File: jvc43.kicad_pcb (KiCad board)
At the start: 6 copper layers, 101.6 x 50.8 mm, 143 parts, among them J201 8P8C_LED_Shielded, J301 8P8C_LED_Shielded, J401 USB_C_Receptacle_USB2.0, U201 LAN8810, U301 LAN8810, U401 LTC3622*DE, X101 25 MHz

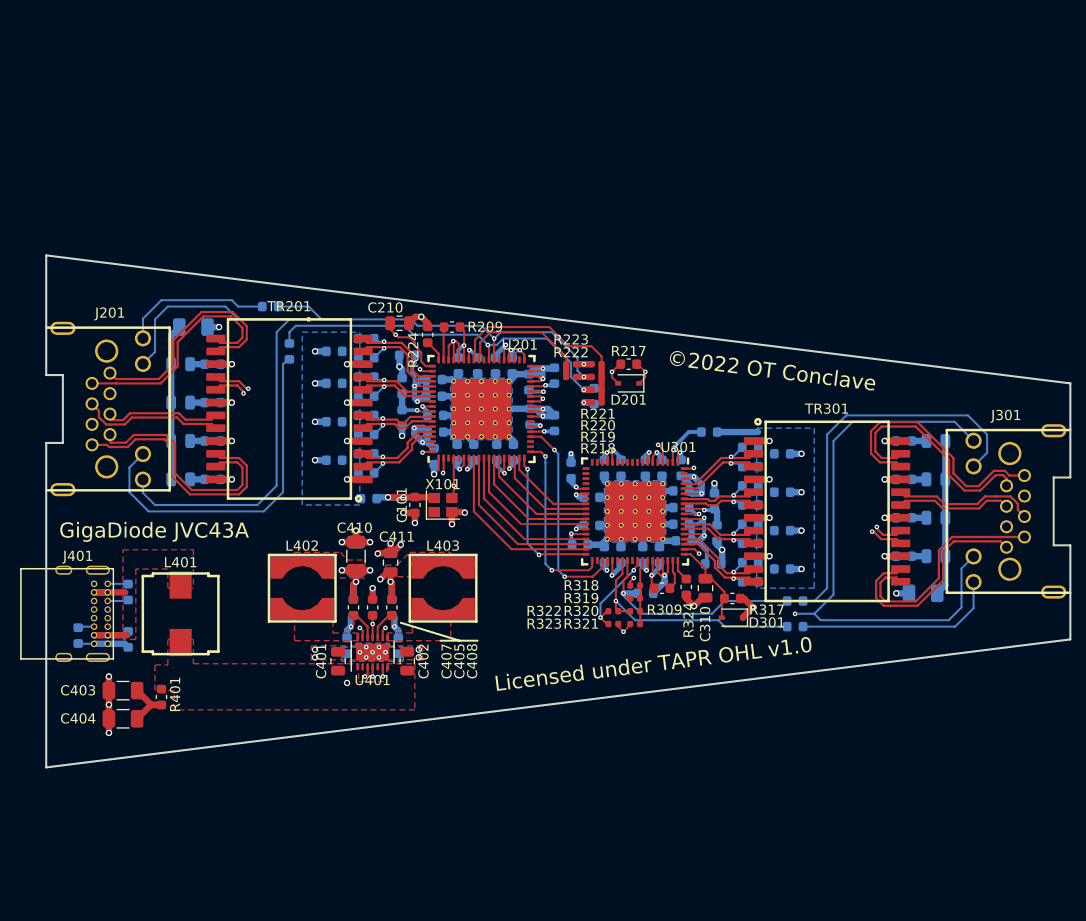
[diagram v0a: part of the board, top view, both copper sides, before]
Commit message: Forward progress: - Ripped up a good chunk of the old place&route around the PHYs - Swizzled graphical placement of LAN8831 diff pair pins, to make the trace   routing be straight-thru.  This also involved swapping the polarity I'm   feeding into the magnetics.  Bonus: the magnetics-to-RJ45 is now straight,   instead of having to go around the back sides! - Adjusted some default trace spacings because of the tiny 0.4mm QFN:   - Switched default traces from 8mil to 7.8mil   - Switched diff pairs from 8.8/8.1 to 7.4/7.8 - Whoops, not all the 0.1uF decoupling caps were 0402 sized yet - Filled in a lot of specific vendor P/Ns for resistors & capacitors, to make   dealing with assembly houses easier
PHY1 has all its close-in decoupling caps placed & routed, PHY2 does not yet.
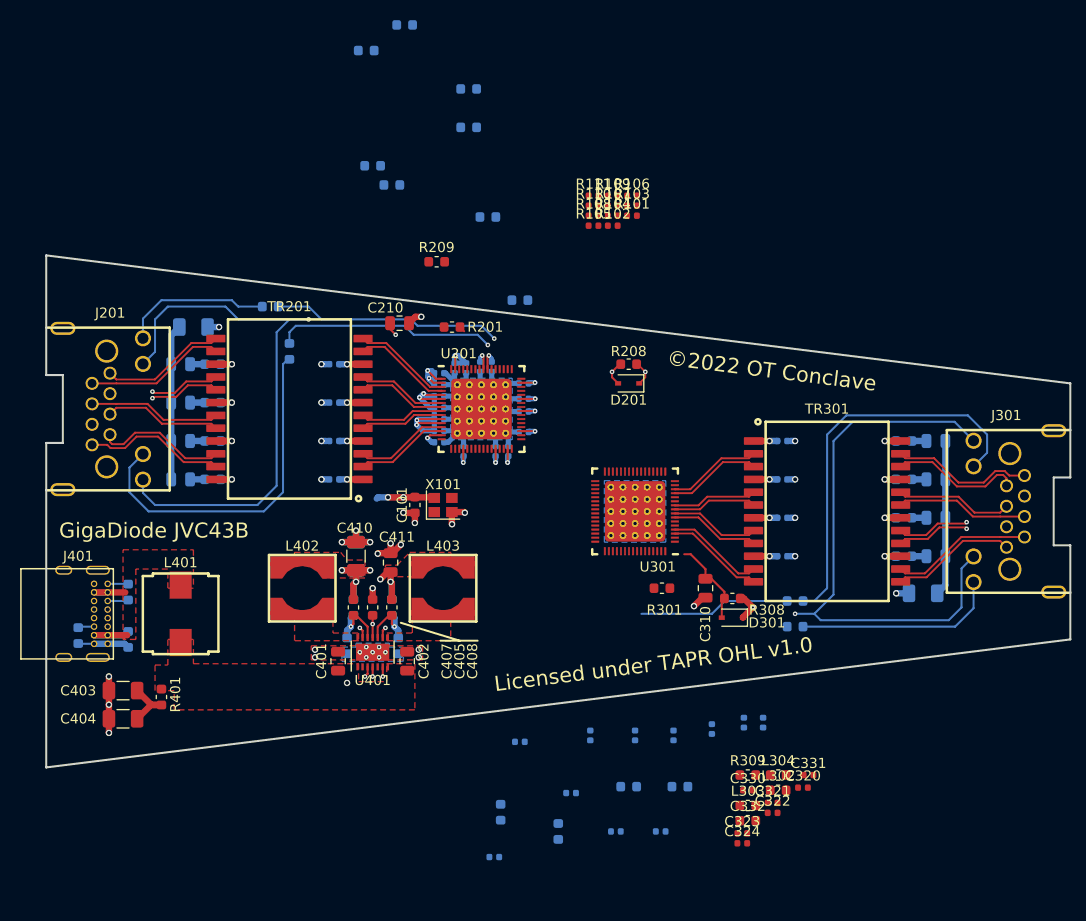
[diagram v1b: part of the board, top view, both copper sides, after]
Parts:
- removed the L201 at (57.4, 49.5)
- removed the L301 at (91.2, 42.9)
- removed the R201 at (57.1, 33.7)
- removed the R202 at (57.1, 35.6)
- removed the R203 at (57.1, 37.5)
- removed the R204 at (57.1, 39.4)
- removed the R205 at (57.1, 41.3)
- removed the R206 at (57.1, 43.2)
- removed the R207 at (57.1, 45.1)
- removed the R208 at (57.1, 47.0)
- removed R216, R316: 5k1, Resistor_SMD:R_0603_1608Metric
- removed R218, R223, R318, R323: 0, Resistor_SMD:R_0402_1005Metric
- removed R219, R220, R221, R222, R319, R320, R321, R322: dnp, Resistor_SMD:R_0402_1005Metric
- removed R224, R324: 8.06k, Resistor_SMD:R_0603_1608Metric
- removed the R301 at (95.2, 57.8)
- removed the R302 at (95.2, 55.9)
- removed the R303 at (95.2, 54.0)
- removed the R304 at (95.2, 52.1)
- removed the R305 at (95.2, 50.2)
- removed the R306 at (95.2, 48.3)
- removed the R307 at (95.2, 46.4)
- removed the R308 at (95.2, 44.5)
- added C225: 0.1u, Capacitor_SMD:C_0402_1005Metric, B.Cu at (64.4, 39.4)
- added C230: 10n, Capacitor_SMD:C_0402_1005Metric, B.Cu at (65.9, 36.6)
- added C231: 0.1u, Capacitor_SMD:C_0402_1005Metric, B.Cu at (67.1, 36.6)
- added C232: 4.7u, Capacitor_SMD:C_0603_1608Metric, B.Cu at (61.0, 2.54)
- added C325: 0.1u, Capacitor_SMD:C_0402_1005Metric, B.Cu at (91.4, 72.4)
- added C330: 10n, Capacitor_SMD:C_0402_1005Metric, F.Cu at (95.0, 78.5)
- added C331: 0.1u, Capacitor_SMD:C_0402_1005Metric, F.Cu at (101.0, 77.0)
- added C332: 4.7u, Capacitor_SMD:C_0603_1608Metric, F.Cu at (95.0, 81.5)
- added L202: 470 ohm, Inductor_SMD:L_0603_1608Metric, B.Cu at (67.3, 12.7)
- added L204: 470 ohm, Inductor_SMD:L_0603_1608Metric, B.Cu at (57.1, 5.08)
- added L302: 470 ohm, Inductor_SMD:L_0603_1608Metric, F.Cu at (98.0, 78.5)
- added L304: 470 ohm, Inductor_SMD:L_0603_1608Metric, F.Cu at (98.0, 77.0)
- added R101: 22, Resistor_SMD:R_0402_1005Metric, F.Cu at (83.5, 21.5)
- added R102: 22, Resistor_SMD:R_0402_1005Metric, F.Cu at (81.6, 22.5)
- added R103: 22, Resistor_SMD:R_0402_1005Metric, F.Cu at (83.5, 20.5)
- added R104: 22, Resistor_SMD:R_0402_1005Metric, F.Cu at (81.6, 21.5)
- added R105: 22, Resistor_SMD:R_0402_1005Metric, F.Cu at (79.7, 22.5)
- added R106: 22, Resistor_SMD:R_0402_1005Metric, F.Cu at (83.5, 19.5)
- added R107: 22, Resistor_SMD:R_0402_1005Metric, F.Cu at (81.6, 20.5)
- added R108: 22, Resistor_SMD:R_0402_1005Metric, F.Cu at (79.7, 21.5)
- added R109: 22, Resistor_SMD:R_0402_1005Metric, F.Cu at (81.6, 19.5)
- added R110: 22, Resistor_SMD:R_0402_1005Metric, F.Cu at (79.7, 20.5)
- added R111: 22, Resistor_SMD:R_0402_1005Metric, F.Cu at (79.7, 19.5)
- added R209: 6.04k, Resistor_SMD:R_0603_1608Metric, F.Cu at (64.1, 26.0)
- added R309: 6.04k, Resistor_SMD:R_0603_1608Metric, F.Cu at (95.0, 77.0)
- C201, C202, C203, C204, C301, C302, C303, C304: value 22n -> 0.1u; footprint Capacitor_SMD:C_0603_1608Metric -> Capacitor_SMD:C_0402_1005Metric
- C211, C219, C311, C319: value 10n -> 10u
- C212, C213, C214, C215, C216, C217, C218, C220, C221, C222, C223, C224, C226, C227, C228, C312, C313, C314, C315, C316, C317, C318, C326, C327, C328: value 10n -> 0.1u; footprint Capacitor_SMD:C_0603_1608Metric -> Capacitor_SMD:C_0402_1005Metric
- C229: renamed from C225; value 10n -> 10u
- C320, C321, C322, C323, C324: value 10n -> 0.1u; footprint Capacitor_SMD:C_0603_1608Metric -> Capacitor_SMD:C_0402_1005Metric; moved to F.Cu
- C329: renamed from C325; value 10n -> 10u
- L303: moved to F.Cu
- R208: renamed from R217; value 5k1 -> 10k
- R308: renamed from R317; value 5k1 -> 10k
- R404: value 100k -> 84.5k
- U201, U301: value LAN8810 -> LAN8831; footprint myfp:QFN-72-1EP_10x10mm_P0.5mm_EP6x6mm_ThermalVias -> myfp:QFN-64-1EP_8x8mm_P0.4mm_EP6x6mm_ThermalVias
- moved C313 40.8 mm to (69.8, 85.1)
- moved C322 38.1 mm to (97.5, 80.7), turned to 0 degrees
- moved C323 36.5 mm to (94.5, 82.7)
- moved C321 35.6 mm to (97.5, 79.7), turned to 0 degrees
- moved C324 34.9 mm to (94.5, 83.7)
- moved C328 33.2 mm to (86.4, 82.5), turned to 0 degrees
- moved L203 30.2 mm to (67.3, 8.89), turned to 0 degrees
- moved C312 28.8 mm to (77.5, 78.7)
- moved C318 28.7 mm to (81.9, 82.5)
- moved C327 28.2 mm to (72.4, 73.7), turned to 0 degrees
- moved C319 28.2 mm to (70.5, 80.6)
- moved C329 27.8 mm to (76.2, 82.5)
- moved L303 27.2 mm to (95.0, 80.0), turned to 0 degrees
- moved C320 27.1 mm to (100.5, 78.2), turned to 0 degrees
- moved C316 27.0 mm to (87.6, 73.0)
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- renumbered L202 to L201, L302 to L301, R209 to R201, R210 to R202, R211 to R203, R212 to R204, R213 to R205, R214 to R206, R215 to R207, R309 to R301, R310 to R302, R311 to R303, R312 to R304, R313 to R305, R314 to R306, R315 to R307
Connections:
- C201 pad 1: /Ethernet1/VDD_ETH -> /Ethernet1/ETH_CR3
- C202 pad 1: /Ethernet1/VDD_ETH -> /Ethernet1/ETH_CR2
- C203 pad 1: /Ethernet1/VDD_ETH -> /Ethernet1/ETH_CR1
- C204 pad 1: /Ethernet1/VDD_ETH -> /Ethernet1/ETH_CR0
- C211 pad 1: /Ethernet1/VDD12A -> /Ethernet1/VDDAH
- C212 pad 1: /Ethernet1/VDD12A -> /Ethernet1/VDDAH
- C213 pad 1: /Ethernet1/VDD12A -> /Ethernet1/VDDAH
- C214 pad 1: /Ethernet1/VDD12A -> /Ethernet1/VDDAH
- C215 pad 1: +2V5 -> /Ethernet1/VDD
- C216 pad 1: +2V5 -> /Ethernet1/VDD
- C217 pad 1: +2V5 -> /Ethernet1/VDD
- C218 pad 1: +2V5 -> /Ethernet1/VDD
- C219 pad 1: +2V5 -> /Ethernet1/VDD
- C221 pad 1: +1V2 -> +2V5
- C222 pad 1: +1V2 -> +2V5
- C223 pad 1: +1V2 -> +2V5
- C224 pad 1: +1V2 -> +2V5
- C226 pad 1: +1V2 -> /Ethernet1/VDDAL
- C227 pad 1: +1V2 -> /Ethernet1/VDDAL
- C228 pad 1: /Ethernet1/VDD12PLL -> /Ethernet1/VDDAL
- C229 pad 1: +1V2 -> /Ethernet1/VDDAL
- C301 pad 1: /Ethernet2/VDD_ETH -> /Ethernet2/ETH_CR3
- C302 pad 1: /Ethernet2/VDD_ETH -> /Ethernet2/ETH_CR2
- C303 pad 1: /Ethernet2/VDD_ETH -> /Ethernet2/ETH_CR1
- C304 pad 1: /Ethernet2/VDD_ETH -> /Ethernet2/ETH_CR0
- C311 pad 1: /Ethernet2/VDD12A -> /Ethernet2/VDDAH
- C312 pad 1: /Ethernet2/VDD12A -> /Ethernet2/VDDAH
- C313 pad 1: /Ethernet2/VDD12A -> /Ethernet2/VDDAH
- C314 pad 1: /Ethernet2/VDD12A -> /Ethernet2/VDDAH
- C315 pad 1: +2V5 -> /Ethernet2/VDD
- C316 pad 1: +2V5 -> /Ethernet2/VDD
- C317 pad 1: +2V5 -> /Ethernet2/VDD
- C318 pad 1: +2V5 -> /Ethernet2/VDD
- C319 pad 1: +2V5 -> /Ethernet2/VDD
- C321 pad 1: +1V2 -> +2V5
- C322 pad 1: +1V2 -> +2V5
- C323 pad 1: +1V2 -> +2V5
- C324 pad 1: +1V2 -> +2V5
- C326 pad 1: +1V2 -> /Ethernet2/VDDAL
- C327 pad 1: +1V2 -> /Ethernet2/VDDAL
- C328 pad 1: /Ethernet2/VDD12PLL -> /Ethernet2/VDDAL
- C329 pad 1: +1V2 -> /Ethernet2/VDDAL
- C407 pad 1: +1V2 -> +1V1
- C409 pad 1: +1V2 -> +1V1
- C410 pad 1: +1V2 -> +1V1
- L201 pad 1: +1V2 -> +2V5
- L201 pad 2: /Ethernet1/VDD12A -> /Ethernet1/VDDAH
- L203 pad 1: +1V2 -> /Ethernet1/VDDAL
- L203 pad 2: /Ethernet1/VDD12PLL -> +1V1
- L301 pad 1: +1V2 -> +2V5
- L301 pad 2: /Ethernet2/VDD12A -> /Ethernet2/VDDAH
- L303 pad 1: +1V2 -> /Ethernet2/VDDAL
- L303 pad 2: /Ethernet2/VDD12PLL -> +1V1
- L402 pad 1: +1V2 -> +1V1
- R201 pad 2: +2V5 -> /Ethernet1/VDDVARIO
- R301 pad 2: +2V5 -> /Ethernet2/VDDVARIO
- R404 pad 1: +1V2 -> +1V1
- TR201 pad 1: /Ethernet1/VDD_ETH -> /Ethernet1/ETH_CR3
- TR201 pad 10: /Ethernet1/VDD_ETH -> /Ethernet1/ETH_CR0
- TR201 pad 11: /Ethernet1/ETH_TR0+ -> /Ethernet1/ETH_TR0-
- TR201 pad 12: /Ethernet1/ETH_TR0- -> /Ethernet1/ETH_TR0+
- TR201 pad 13: /Ethernet1/ETH_TX0- -> /Ethernet1/ETH_TX0+
- TR201 pad 14: /Ethernet1/ETH_TX0+ -> /Ethernet1/ETH_TX0-
- TR201 pad 16: /Ethernet1/ETH_TX1- -> /Ethernet1/ETH_TX1+
- TR201 pad 17: /Ethernet1/ETH_TX1+ -> /Ethernet1/ETH_TX1-
- TR201 pad 19: /Ethernet1/ETH_TX2- -> /Ethernet1/ETH_TX2+
- TR201 pad 2: /Ethernet1/ETH_TR3+ -> /Ethernet1/ETH_TR3-
- TR201 pad 20: /Ethernet1/ETH_TX2+ -> /Ethernet1/ETH_TX2-
- TR201 pad 22: /Ethernet1/ETH_TX3- -> /Ethernet1/ETH_TX3+
- TR201 pad 23: /Ethernet1/ETH_TX3+ -> /Ethernet1/ETH_TX3-
- TR201 pad 3: /Ethernet1/ETH_TR3- -> /Ethernet1/ETH_TR3+
- TR201 pad 4: /Ethernet1/VDD_ETH -> /Ethernet1/ETH_CR2
- TR201 pad 5: /Ethernet1/ETH_TR2+ -> /Ethernet1/ETH_TR2-
- TR201 pad 6: /Ethernet1/ETH_TR2- -> /Ethernet1/ETH_TR2+
- TR201 pad 7: /Ethernet1/VDD_ETH -> /Ethernet1/ETH_CR1
- TR201 pad 8: /Ethernet1/ETH_TR1+ -> /Ethernet1/ETH_TR1-
- TR201 pad 9: /Ethernet1/ETH_TR1- -> /Ethernet1/ETH_TR1+
- TR301 pad 1: /Ethernet2/VDD_ETH -> /Ethernet2/ETH_CR3
- TR301 pad 10: /Ethernet2/VDD_ETH -> /Ethernet2/ETH_CR0
- TR301 pad 11: /Ethernet2/ETH_TR0+ -> /Ethernet2/ETH_TR0-
- TR301 pad 12: /Ethernet2/ETH_TR0- -> /Ethernet2/ETH_TR0+
- TR301 pad 13: /Ethernet2/ETH_TX0- -> /Ethernet2/ETH_TX0+
- TR301 pad 14: /Ethernet2/ETH_TX0+ -> /Ethernet2/ETH_TX0-
- TR301 pad 16: /Ethernet2/ETH_TX1- -> /Ethernet2/ETH_TX1+
- TR301 pad 17: /Ethernet2/ETH_TX1+ -> /Ethernet2/ETH_TX1-
- TR301 pad 19: /Ethernet2/ETH_TX2- -> /Ethernet2/ETH_TX2+
- TR301 pad 2: /Ethernet2/ETH_TR3+ -> /Ethernet2/ETH_TR3-
- TR301 pad 20: /Ethernet2/ETH_TX2+ -> /Ethernet2/ETH_TX2-
- TR301 pad 22: /Ethernet2/ETH_TX3- -> /Ethernet2/ETH_TX3+
- TR301 pad 23: /Ethernet2/ETH_TX3+ -> /Ethernet2/ETH_TX3-
- TR301 pad 3: /Ethernet2/ETH_TR3- -> /Ethernet2/ETH_TR3+
- TR301 pad 4: /Ethernet2/VDD_ETH -> /Ethernet2/ETH_CR2
- TR301 pad 5: /Ethernet2/ETH_TR2+ -> /Ethernet2/ETH_TR2-
- TR301 pad 6: /Ethernet2/ETH_TR2- -> /Ethernet2/ETH_TR2+
- TR301 pad 7: /Ethernet2/VDD_ETH -> /Ethernet2/ETH_CR1
- TR301 pad 8: /Ethernet2/ETH_TR1+ -> /Ethernet2/ETH_TR1-
- TR301 pad 9: /Ethernet2/ETH_TR1- -> /Ethernet2/ETH_TR1+
- U201 pad 1: GND -> /Ethernet1/VDDAH
- U201 pad 10: /Ethernet1/RXD2 -> /Ethernet1/ETH_TR2-
- U201 pad 11: /Ethernet1/RXD3 -> /Ethernet1/VDDAL
- U201 pad 12: /Ethernet1/RXD4 -> /Ethernet1/VDDAL
- U201 pad 13: /Ethernet1/RXD5 -> /Ethernet1/ETH_TR3+
- U201 pad 14: +2V5 -> /Ethernet1/ETH_TR3-
- U201 pad 15: +1V2 -> /Ethernet1/VDDAH
- U201 pad 16: /Ethernet1/RXD6 -> /Ethernet1/LED5
- U201 pad 17: /Ethernet1/RXD7 -> /Ethernet1/LED4
- U201 pad 18: /EN_W2B -> /Ethernet1/LED3
- U201 pad 19: /ER_W2B -> /Ethernet1/LED2
- U201 pad 2: +2V5 -> /Ethernet1/VDDAH
- U201 pad 20: /Ethernet1/CRS -> +2V5
- U201 pad 21: /Ethernet1/COL -> /Ethernet1/LED1
- U201 pad 22: /CLK_W2B -> GND
- U201 pad 23: +2V5 -> GND
- U201 pad 24: +1V2 -> GND
- U201 pad 25: Net-(U201-Pad25) -> GND
- U201 pad 28: GND -> /Ethernet1/VDD
- U201 pad 3: /Ethernet1/TDO -> /Ethernet1/ETH_TR0+
- U201 pad 31: +1V2 -> +2V5
- U201 pad 32: +2V5 -> GND
- U201 pad 35: GND -> /Ethernet1/VDD
- U201 pad 36: GND -> /RXD7
- U201 pad 37: GND -> /RXD6
- U201 pad 38: /Ethernet1/TXCLK -> /RXD5
- U201 pad 39: GND -> /RXD4
- U201 pad 4: /Ethernet1/XI -> /Ethernet1/ETH_TR0-
- U201 pad 40: +1V2 -> +2V5
- U201 pad 41: +2V5 -> /RXD3
- U201 pad 42: /Ethernet1/ACT_LED -> /RXD2
- U201 pad 43: /Ethernet1/1000_LED -> /Ethernet1/VDD
- U201 pad 44: /Ethernet1/100_LED -> /RXD1
- U201 pad 45: /Ethernet1/10_LED -> /RXD0
- U201 pad 46: /Ethernet1/CONFIG3 -> /Ethernet1/RXDV
- U201 pad 47: /Ethernet1/CONFIG2 -> +2V5
- U201 pad 48: +1V2 -> /Ethernet1/RXER
- U201 pad 49: +2V5 -> /Ethernet1/RXCLK
- U201 pad 5: /Ethernet1/XO -> /Ethernet1/VDDAL
- U201 pad 50: GND -> /Ethernet1/CRS
- U201 pad 52: GND -> /Ethernet1/MDIO
- U201 pad 53: /Ethernet1/MDIO -> /Ethernet1/COL
- U201 pad 54: /Ethernet1/ETHRBIAS -> /Ethernet1/INT
- U201 pad 55: /Ethernet1/nRST -> /Ethernet1/VDD
- U201 pad 56: GND -> +2V5
- U201 pad 57: /Ethernet1/ETH_TR0- -> /Ethernet1/CLK125
- U201 pad 58: /Ethernet1/ETH_TR0+ -> /Ethernet1/nRST
- U201 pad 59: /Ethernet1/VDD12A -> /Ethernet1/TXCLK
- U201 pad 6: +2V5 -> /Ethernet1/VDDAL
- U201 pad 60: /Ethernet1/ETH_TR1- -> Net-(U201-Pad60)
- U201 pad 61: /Ethernet1/ETH_TR1+ -> /Ethernet1/XO
- U201 pad 62: /Ethernet1/VDD12A -> /Ethernet1/XI
- U201 pad 63: +1V2 -> /Ethernet1/VDDAL_PLL
- U201 pad 64: /Ethernet1/VDD12PLL -> /Ethernet1/ISET
- U201 pad 7: +1V2 -> /Ethernet1/ETH_TR1+
- U201 pad 8: /Ethernet1/RXD0 -> /Ethernet1/ETH_TR1-
- U201 pad 9: /Ethernet1/RXD1 -> /Ethernet1/ETH_TR2+
- U301 pad 1: GND -> /Ethernet2/VDDAH
- U301 pad 10: /Ethernet2/RXD2 -> /Ethernet2/ETH_TR2-
- U301 pad 11: /Ethernet2/RXD3 -> /Ethernet2/VDDAL
- U301 pad 12: /Ethernet2/RXD4 -> /Ethernet2/VDDAL
- U301 pad 13: /Ethernet2/RXD5 -> /Ethernet2/ETH_TR3+
- U301 pad 14: +2V5 -> /Ethernet2/ETH_TR3-
- U301 pad 15: +1V2 -> /Ethernet2/VDDAH
- U301 pad 16: /Ethernet2/RXD6 -> /Ethernet2/LED5
- U301 pad 17: /Ethernet2/RXD7 -> /Ethernet2/LED4
- U301 pad 18: /Ethernet2/RXDV -> /Ethernet2/LED3
- U301 pad 19: /Ethernet2/RXER -> /Ethernet2/LED2
- U301 pad 2: +2V5 -> /Ethernet2/VDDAH
- U301 pad 20: /Ethernet2/CRS -> +2V5
- U301 pad 21: /Ethernet2/COL -> /Ethernet2/LED1
- U301 pad 22: /Ethernet2/RXCLK -> /TXD0
- U301 pad 23: +2V5 -> /TXD1
- U301 pad 24: +1V2 -> /TXD2
- U301 pad 25: Net-(U301-Pad25) -> /TXD3
- U301 pad 26: /Ethernet1/RXD7 -> /TXD4
- U301 pad 27: /Ethernet1/RXD6 -> /TXD5
- U301 pad 28: /Ethernet1/RXD5 -> /Ethernet2/VDD
- U301 pad 29: /Ethernet1/RXD4 -> /TXD6
- U301 pad 3: /Ethernet2/TDO -> /Ethernet2/ETH_TR0+
- U301 pad 30: /Ethernet1/RXD3 -> /TXD7
- U301 pad 31: +1V2 -> +2V5
- U301 pad 32: +2V5 -> /ER_W2B
- U301 pad 33: /Ethernet1/RXD2 -> /CLK_W2B
- U301 pad 34: /Ethernet1/RXD1 -> /EN_W2B
- U301 pad 35: /Ethernet1/RXD0 -> /Ethernet2/VDD
- U301 pad 36: /EN_W2B -> /Ethernet2/RXD7
- U301 pad 37: /ER_W2B -> /Ethernet2/RXD6
- U301 pad 38: /Ethernet2/TXCLK -> /Ethernet2/RXD5
- U301 pad 39: /CLK_W2B -> /Ethernet2/RXD4
- U301 pad 4: /Ethernet1/XI -> /Ethernet2/ETH_TR0-
- U301 pad 40: +1V2 -> +2V5
- U301 pad 41: +2V5 -> /Ethernet2/RXD3
- U301 pad 42: /Ethernet2/ACT_LED -> /Ethernet2/RXD2
- U301 pad 43: /Ethernet2/1000_LED -> /Ethernet2/VDD
- U301 pad 44: /Ethernet2/100_LED -> /Ethernet2/RXD1
- U301 pad 45: /Ethernet2/10_LED -> /Ethernet2/RXD0
- U301 pad 46: /Ethernet2/CONFIG3 -> /Ethernet2/RXDV
- U301 pad 47: /Ethernet2/CONFIG2 -> +2V5
- U301 pad 48: +1V2 -> /Ethernet2/RXER
- U301 pad 49: +2V5 -> /Ethernet2/RXCLK
- U301 pad 5: /Ethernet2/XO -> /Ethernet2/VDDAL
- U301 pad 50: GND -> /Ethernet2/CRS
- U301 pad 52: GND -> /Ethernet2/MDIO
- U301 pad 53: /Ethernet2/MDIO -> /Ethernet2/COL
- U301 pad 54: /Ethernet2/ETHRBIAS -> /Ethernet2/INT
- U301 pad 55: /Ethernet2/nRST -> /Ethernet2/VDD
- U301 pad 56: GND -> +2V5
- U301 pad 57: /Ethernet2/ETH_TR0- -> /Ethernet2/CLK125
- U301 pad 58: /Ethernet2/ETH_TR0+ -> /Ethernet2/nRST
- U301 pad 59: /Ethernet2/VDD12A -> /Ethernet2/TXCLK
- U301 pad 6: +2V5 -> /Ethernet2/VDDAL
- U301 pad 60: /Ethernet2/ETH_TR1- -> Net-(U301-Pad60)
- U301 pad 61: /Ethernet2/ETH_TR1+ -> /Ethernet2/XO
- U301 pad 62: /Ethernet2/VDD12A -> /Ethernet1/XI
- U301 pad 63: +1V2 -> /Ethernet2/VDDAL_PLL
- U301 pad 64: /Ethernet2/VDD12PLL -> /Ethernet2/ISET
- U301 pad 7: +1V2 -> /Ethernet2/ETH_TR1+
- U301 pad 8: /Ethernet2/RXD0 -> /Ethernet2/ETH_TR1-
- U301 pad 9: /Ethernet2/RXD1 -> /Ethernet2/ETH_TR2+
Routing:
- net GND: track 239.9 -> 165.0 mm, vias 56 -> 39
- net +1V2: track 45.7 -> 0.00 mm, vias 19 -> 0
- net +2V5: track 66.1 -> 29.0 mm, vias 24 -> 11
- net /Ethernet1/XI: track 28.1 -> 0.00 mm, vias 2 -> 0
- net /Ethernet2/1000_LED: track 24.6 -> 0.00 mm, vias 1 -> 0
- net /Ethernet2/VDD12A: track 22.8 -> 0.00 mm, vias 4 -> 0
- net /Ethernet1/VDD12A: track 21.7 -> 0.00 mm, vias 4 -> 0
- net /Ethernet1/CONFIG2: track 20.9 -> 0.00 mm
- net /CLK_W2B: track 20.7 -> 0.00 mm, vias 2 -> 0
- net /Ethernet1/VDDAL: track 0.00 -> 20.4 mm, vias 0 -> 4
- net /ER_W2B: track 18.0 -> 0.00 mm, vias 2 -> 0
- net /Ethernet1/RXD0: track 18.0 -> 0.00 mm
- net /Ethernet1/RXD1: track 16.9 -> 0.00 mm
- net /Ethernet1/100_LED: track 38.0 -> 21.9 mm, vias 2 -> 1
- net /Ethernet1/RXD2: track 15.8 -> 0.00 mm
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- added copper zone on F.Cu, net +1V1
- added copper zone on L3.Cu, net +1V1
- removed copper zone on F.Cu, net +1V2
- removed copper zone on L3.Cu, net +1V2
- removed copper zone on L4.Cu, net /Ethernet1/VDD12A
- removed copper zone on B.Cu, net /Ethernet1/VDD_ETH
- removed copper zone on L4.Cu, net /Ethernet2/VDD12A
- removed copper zone on B.Cu, net /Ethernet2/VDD_ETH
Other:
- net class Default: clearance 0.2032 -> 0.19812; trace_width 0.2032 -> 0.19812
- net class Diff100: clearance 0.20574 -> 0.19812; trace_width 0.22352 -> 0.18796
- net class Phat25: clearance 0.2032 -> 0.19812
- net class UghClear removed
- rule trace_clearance: 0.2032 -> 0.19812
- board text added: "(11) IMPEDANCE: ALL 7.4 MIL WIDE / 7.8 MIL SPACE PAIRS ON LAYERS F/3 SHALL BE 100 OHMS +/- 10%. REFERENCE LAYER 2."
- board text added: "GigaDiode JVC43B"
- board text removed: "(11) IMPEDANCE: ALL 8.8 MIL WIDE / 8.1 MIL SPACE PAIRS ON LAYERS F/3 SHALL BE 100 OHMS +/- 10%. REFERENCE LAYER 2."
- board text removed: "GigaDiode JVC43A"

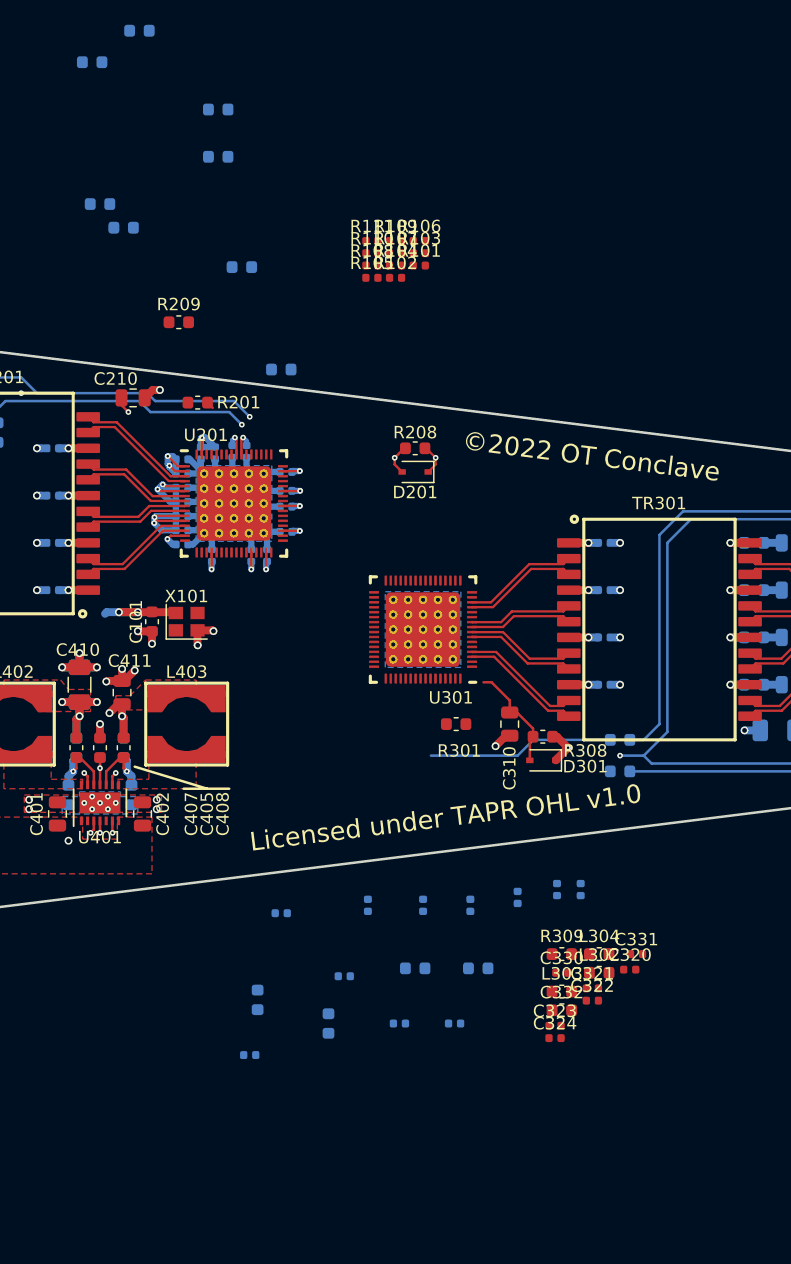
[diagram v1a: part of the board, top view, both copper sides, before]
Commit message: - Sanitized some of the capacitor voltages / footprints - Selected mfr P/Ns for *all* parts - Placed and routed most of the series resistors, ran into a problem with the   VDD vias on PHY1..... - Placed and routed (all?) the bypass caps for PHY2
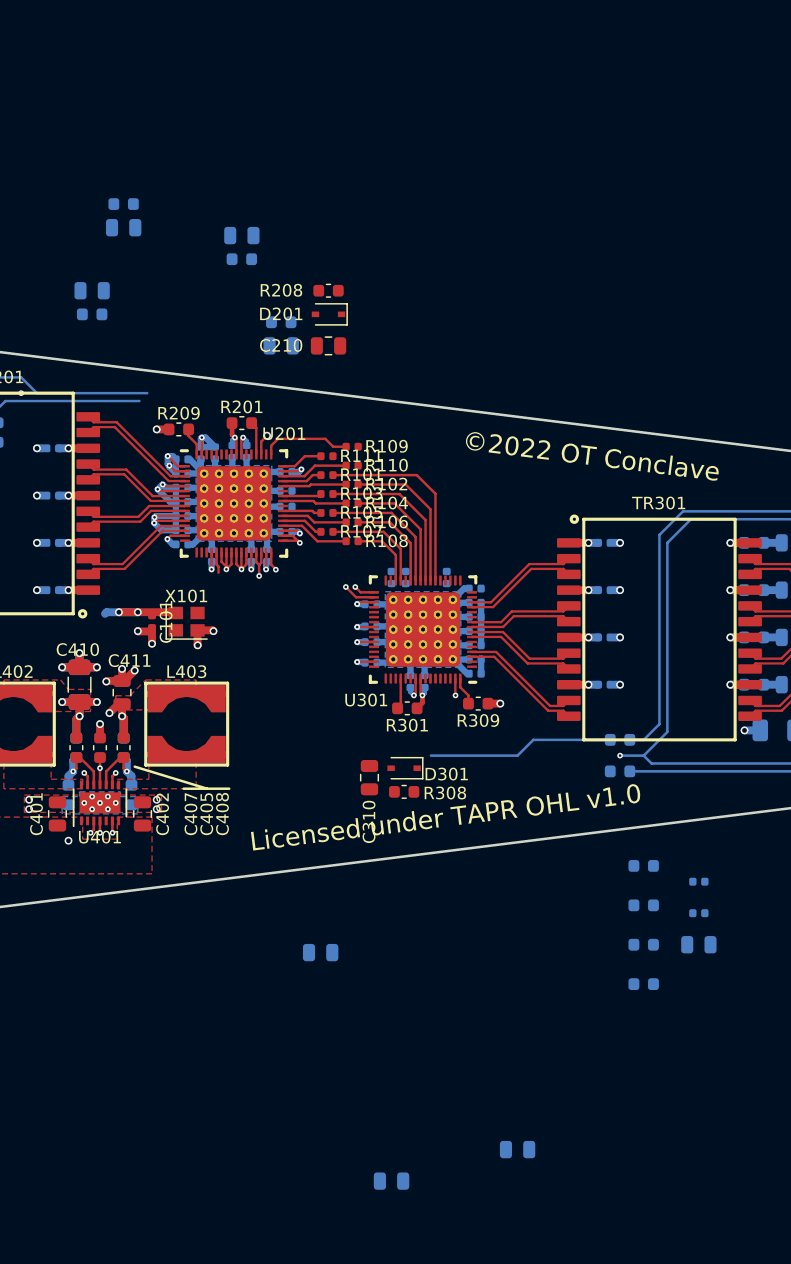
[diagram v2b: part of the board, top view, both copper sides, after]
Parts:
- C101: value 10n -> 0.1u; footprint Capacitor_SMD:C_0603_1608Metric -> Capacitor_SMD:C_0402_1005Metric
- C211, C219, C229, C232, C311, C319, C329: footprint Capacitor_SMD:C_0603_1608Metric -> Capacitor_SMD:C_0805_2012Metric
- C320, C321, C322, C323, C324, C330, C331, L302, L303, L304: moved to B.Cu
- C332: footprint Capacitor_SMD:C_0603_1608Metric -> Capacitor_SMD:C_0805_2012Metric; moved to B.Cu
- R402, R403: value 5k1 -> 5.1k
- moved C321 36.9 mm to (81.3, 46.6), turned to 270 degrees
- moved C313 36.7 mm to (88.0, 53.2)
- moved C322 35.0 mm to (79.6, 50.5)
- moved C320 34.9 mm to (85.7, 46.6), turned to 270 degrees
- moved C328 33.9 mm to (88.0, 48.6), turned to 180 degrees
- moved C323 32.8 mm to (79.6, 53.5)
- moved C324 30.6 mm to (83.9, 55.0), turned to 90 degrees
- moved C327 28.5 mm to (88.0, 49.8), turned to 180 degrees
- moved C315 27.9 mm to (82.4, 46.6)
- moved C318 27.6 mm to (82.8, 55.0), turned to 90 degrees
- moved C312 26.6 mm to (88.0, 54.4)
- moved C314 25.7 mm to (88.0, 47.5), turned to 180 degrees
- moved C316 25.5 mm to (79.6, 48.8), turned to 0 degrees
- moved R106 23.3 mm to (78.1, 42.2), turned to 180 degrees
- moved R107 23.1 mm to (76.1, 42.9), turned to 180 degrees
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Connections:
- net Net-(U201-Pad60) renamed /Ethernet1/LDO_O
- net Net-(U301-Pad60) renamed /Ethernet2/LDO_O
- R201 pad 2: /Ethernet1/VDDVARIO -> +2V5
- R301 pad 2: /Ethernet2/VDDVARIO -> +2V5
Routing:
- net GND: track 165.0 -> 194.1 mm, vias 39 -> 45
- net /Ethernet1/nRST: track 27.1 -> 0.00 mm, vias 2 -> 0
- net /TXD0: track 0.00 -> 15.9 mm
- net /TXD2: track 0.00 -> 13.2 mm
- net /TXD1: track 0.00 -> 12.4 mm
- net /TXD4: track 0.00 -> 11.0 mm
- net /TXD3: track 0.00 -> 10.0 mm
- net /Ethernet1/1000_LED: track 22.8 -> 13.7 mm, vias 1 -> 0
- net /Ethernet1/100_LED: track 21.9 -> 12.8 mm, vias 1 -> 0
- net /Ethernet2/nRST: track 8.78 -> 0.00 mm
- net /TXD6: track 0.00 -> 8.58 mm
- net /TXD5: track 0.00 -> 7.94 mm
- net /Ethernet1/RXCLK: track 0.00 -> 7.23 mm
- net /Ethernet2/VDD: track 0.00 -> 6.22 mm, vias 0 -> 3
- net /RXD7: track 0.00 -> 5.61 mm
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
